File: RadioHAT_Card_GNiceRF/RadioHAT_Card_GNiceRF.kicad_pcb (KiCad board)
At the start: 2 copper layers, 30 x 51 mm, 10 parts, among them J2 Conn_Coaxial, J3 Conn_Coaxial, J4 Conn_Coaxial, J5 Conn_Coaxial, J6 Conn_Coaxial

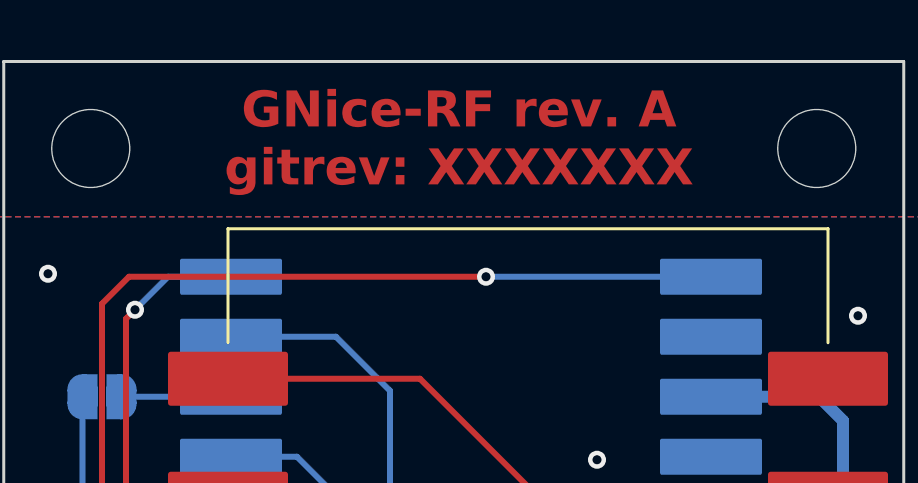
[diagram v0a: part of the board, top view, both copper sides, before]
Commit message: [PCB] Finalize labels
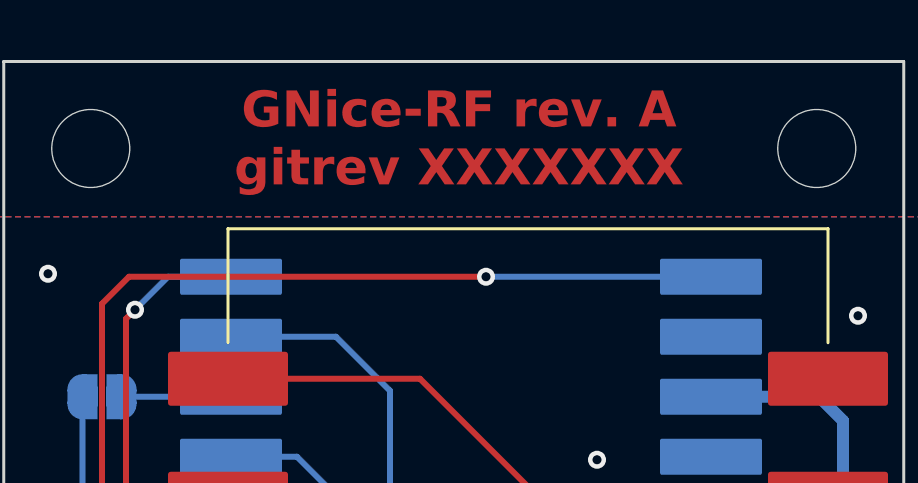
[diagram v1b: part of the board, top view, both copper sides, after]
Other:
- board text added: "GNice-RF rev. A gitrev XXXXXXX"
- board text removed: "GNice-RF rev. A gitrev: XXXXXXX"
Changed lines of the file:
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@@
 		)
 	)
-	(gr_text "GNice-RF rev. A\ngitrev: XXXXXXX"
+	(gr_text "GNice-RF rev. A\ngitrev XXXXXXX"
 		(at 138.4 72 0)
 		(layer "F.Cu")

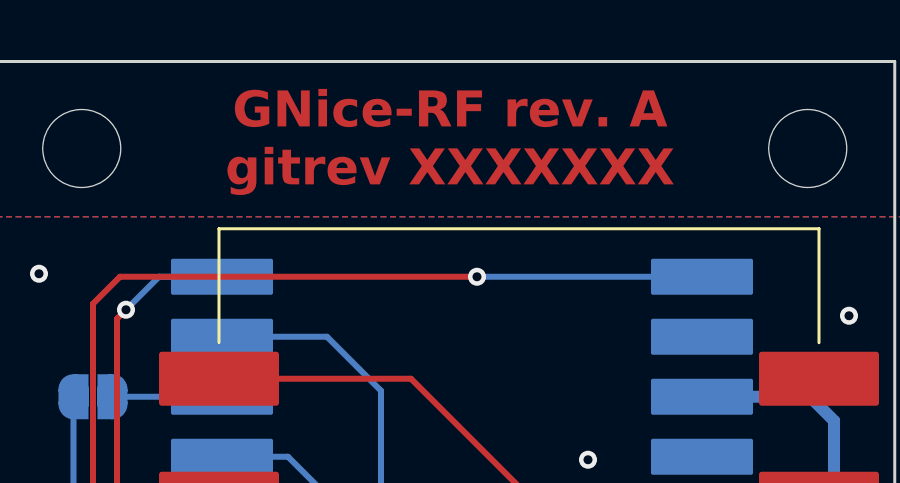
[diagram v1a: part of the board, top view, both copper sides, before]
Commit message: [PCB] Add git hash tag for CI
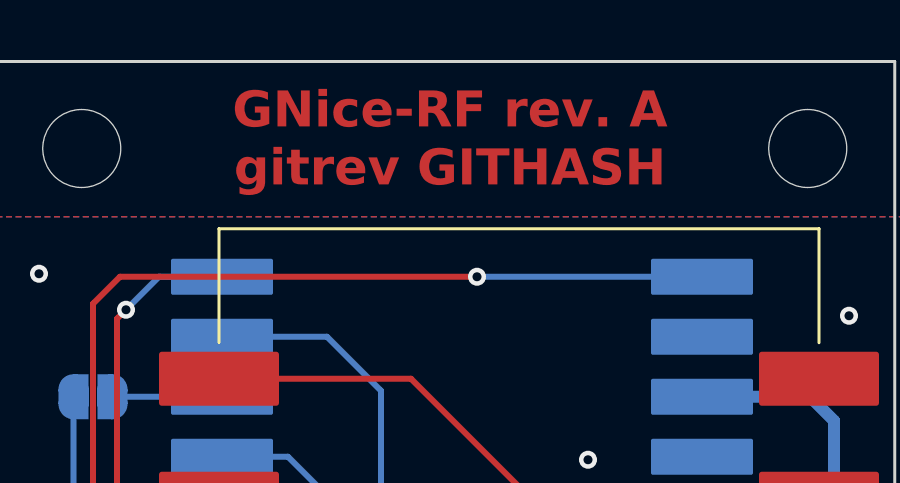
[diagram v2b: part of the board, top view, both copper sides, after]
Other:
- board text added: "GNice-RF rev. A gitrev GITHASH"
- board text removed: "GNice-RF rev. A gitrev XXXXXXX"
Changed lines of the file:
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@@
 		)
 	)
-	(gr_text "GNice-RF rev. A\ngitrev XXXXXXX"
+	(gr_text "GNice-RF rev. A\ngitrev GITHASH"
 		(at 138.4 72 0)
 		(layer "F.Cu")

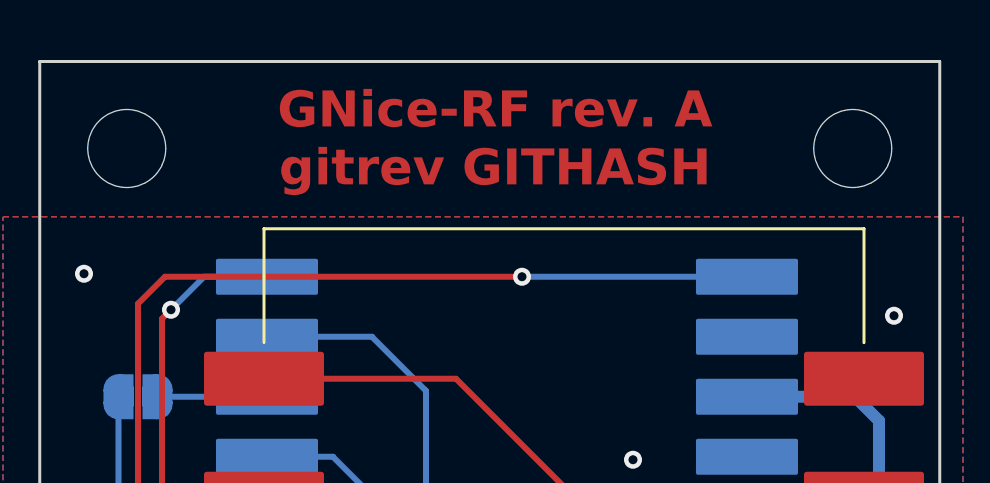
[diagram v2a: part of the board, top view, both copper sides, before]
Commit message: [PCB] Make cards' githash variable
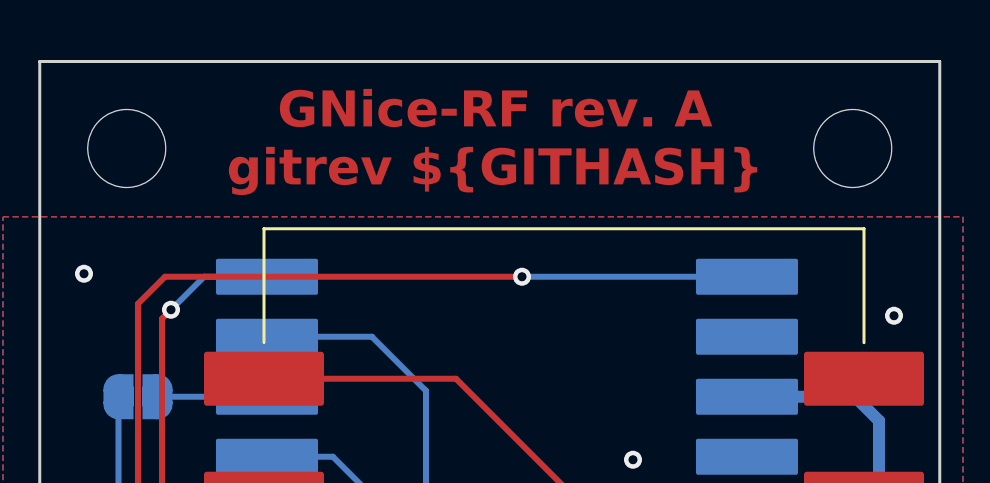
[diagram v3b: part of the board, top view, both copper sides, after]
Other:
- board text added: "GNice-RF rev. A gitrev ${GITHASH}"
- board text removed: "GNice-RF rev. A gitrev GITHASH"
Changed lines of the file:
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@@
 		)
 	)
-	(gr_text "GNice-RF rev. A\ngitrev GITHASH"
+	(gr_text "GNice-RF rev. A\ngitrev ${GITHASH}"
 		(at 138.4 72 0)
 		(layer "F.Cu")

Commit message: [PCB] Fix flipped pinout for 12XXF30
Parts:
- moved J2 24.7 mm to (150.6, 106.0), turned to -90 degrees
- moved U1 5.10 mm to (135.6, 93.9)
- moved JP1 0.30 mm to (126.5, 80.3), turned to -90 degrees
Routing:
- net GPIO1: track 40.5 -> 57.3 mm, vias 3 -> 1
- net NSS: track 51.4 -> 65.1 mm, vias 2 -> 4
- net IRQ1: track 73.8 -> 60.4 mm, vias 1 -> 3
- net MISO: track 64.5 -> 57.6 mm, vias 3 -> 4
- net MOSI: track 61.0 -> 55.2 mm, vias 3 -> 4
- net +3V3: track 85.5 -> 88.7 mm, vias 3 -> 4
- net GPIO0: track 74.1 -> 72.7 mm, vias 4 -> 3
- net SCK: track 64.7 -> 63.7 mm
- net Net-(JP1-B): track 3.65 -> 4.44 mm
- net RST1: track 39.2 -> 39.8 mm, vias 2 -> 0
- net IRQ0: track 68.6 -> 69.1 mm, vias 5 -> 3
- net RST0: track 52.7 -> 53.3 mm
- net GND: vias 16 -> 15
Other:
- board text added: "GNice-RF rev. B gitrev ${GITHASH}"
- board text removed: "GNice-RF rev. A gitrev ${GITHASH}"

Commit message: [PCB] Fix minor DRC issue
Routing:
- net NSS: track 65.1 -> 65.7 mm
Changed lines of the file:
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@@
+	)
+	(segment
+		(start 127.225 114)
+		(end 134 114)
+		(width 0.2)
+		(layer "B.Cu")
+		(net 11)
+	)
+	(segment
+		(start 148.6 97.8)
+		(end 148.925 98.125)
+		(width 0.2)
+		(layer "B.Cu")
+		(net 11)
+	)
+	(segment
+		(start 143.1 104.9)
+		(end 145.8 104.9)
+		(width 0.2)
+		(layer "B.Cu")
+		(net 11)
+	)
+	(segment
+		(start 148.925 98.125)
+		(end 148.925 103.875)
+		(width 0.2)
+		(layer "B.Cu")
+		(net 11)
+	)
+	(segment
+		(start 148.925 103.875)
+		(end 147.9 104.9)
+		(width 0.2)
+		(layer "B.Cu")
+		(net 11)
 	)
 	(segment
@@
 	)
 	(segment
-		(start 127.225 114)
-		(end 134 114)
-		(width 0.2)
-		(layer "B.Cu")
-		(net 11)
-	)
-	(segment
-		(start 148.6 97.8)
-		(end 148.6 104.2)
-		(width 0.2)
-		(layer "B.Cu")
-		(net 11)
-	)
-	(segment
-		(start 143.1 104.9)
-		(end 145.8 104.9)
-		(width 0.2)
-		(layer "B.Cu")
-		(net 11)
-	)
-	(segment
-		(start 148.6 104.2)
-		(end 147.9 104.9)
-		(width 0.2)
-		(layer "B.Cu")
-		(net 11)
-	)
-	(segment
 		(start 135 76.6)
 		(end 130.8 76.6)
@@
 	)
 	(segment
-		(start 149.625 108.925)
-		(end 149.625 118.975)
+		(start 150.1 109.025)
+		(end 149.625 109.5)
 		(width 0.2)
 		(layer "F.Cu")
@@
 	)
 	(segment
+		(start 149.625 109.5)
+		(end 149.625 118.975)
+		(width 0.2)
+		(layer "F.Cu")
+		(net 16)
+	)
+	(segment
 		(start 137.05 85.6)
 		(end 135.35 83.9)
@@
 		(net 16)
 	)
-	(segment
-		(start 149.6 108.9)
-		(end 149.625 108.925)
-		(width 0.2)
-		(layer "F.Cu")
-		(net 16)
-	)
 	(via
 		(at 152.3 98.7)
@@
 	)
 	(via
-		(at 149.6 108.9)
+		(at 150.1 109.025)
 		(size 0.6)
 		(drill 0.3)
@@
 	)
 	(segment
-		(start 149.6 108.9)
+		(start 149.975 108.9)
 		(end 145.8 108.9)
 		(width 0.2)
@@
 	)
 	(segment
-		(start 149.6 101.4)
+		(start 150.1 109.025)
+		(end 149.975 108.9)
+		(width 0.2)
+		(layer "B.Cu")
+		(net 16)
+	)
+	(segment
+		(start 150.1 109.025)
+		(end 150.1 100.9)
+		(width 0.2)
+		(layer "B.Cu")
+		(net 16)
+	)
+	(segment
+		(start 150.1 100.9)
 		(end 152.3 98.7)
 		(width 0.2)
@@
 		(width 0.2)
 		(layer "B.Cu")
-		(net 16)
-	)
-	(segment
-		(start 149.6 108.9)
-		(end 149.6 101.4)
-		(width 0.2)
-		(layer "B.Cu")

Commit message: Update G-NiceRF card to use LRxx21 instead of LR1120
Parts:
- removed J6: Conn_Coaxial, Connector_Coaxial:U.FL_Molex_MCRF_73412-0110_Vertical
- removed U3: ~, RadioHAT:LoRa1120
- added U4: ~, RadioHAT:LoRaxx21, B.Cu at (138.3, 103.0)
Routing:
- net NSS: track 65.7 -> 78.6 mm, vias 4 -> 6
- net Net-(J6-Ext): track 10.1 -> 0.00 mm
- net Net-(J6-In): track 3.86 -> 0.00 mm
- net GPIO0: track 72.7 -> 74.9 mm, vias 3 -> 4
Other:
- board text added: "GNice-RF rev. C gitrev ${GITHASH}"
- board text removed: "GNice-RF rev. B gitrev ${GITHASH}"

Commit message: Add 5V channel to GNiceRF card
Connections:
- J1 pad 2: +3V3 -> unconnected-(J1-3V3-Pad2)
- J1 pad 20: (no net) -> unconnected-(J1-NSS1-Pad20)
- J1 pad 28: (no net) -> unconnected-(J1-5V-Pad28)
- J1 pad 4: GND -> unconnected-(J1-GND-Pad4)
- J1 pad 48: (no net) -> unconnected-(J1-5V-Pad48)
- J1 pad 6: (no net) -> +5V
- U1 pad 1: +3V3 -> +5V
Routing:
- net +5V: track 0.00 -> 14.4 mm, vias 0 -> 1
- net +3V3: track 88.7 -> 80.1 mm
- net GND: track 79.3 -> 74.7 mm, vias 15 -> 21
- net GPIO1: track 57.3 -> 58.0 mm
